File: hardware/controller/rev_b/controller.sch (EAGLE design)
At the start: 96 parts, among them J1 MODULE_CONTROLLER, J14 SOLDERJUMPERTRACE, J15 SOLDERJUMPERTRACE, J2 DM3AT-SF-PEJM5, J3 U.FL-R-SMT, J4 MICRO_USB_B_HIROSE_ZX62-B-5PA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, J5 MICRO_USB_B_HIROSE_ZX62-B-5PA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, J6 TC2030-JLINK-L, J7 TC2030-JLINK-L, J8 JUMPER-3PTH, Q1 MOSFET-NCHANNELSMD, Q2 NX3008PBK, SW1 PTS810SJ, SW2 SIP3240X, U1 SAM4LC8AA, U2 SAM4LC8AA, U3 RXM-GPS-RM-T, U4 FM25CLXXB-DG, U5 TS3USB30E, U6 FTDI234XD, U7 TXS0108EVQFN20, X1 16MHz, X2 16MHz

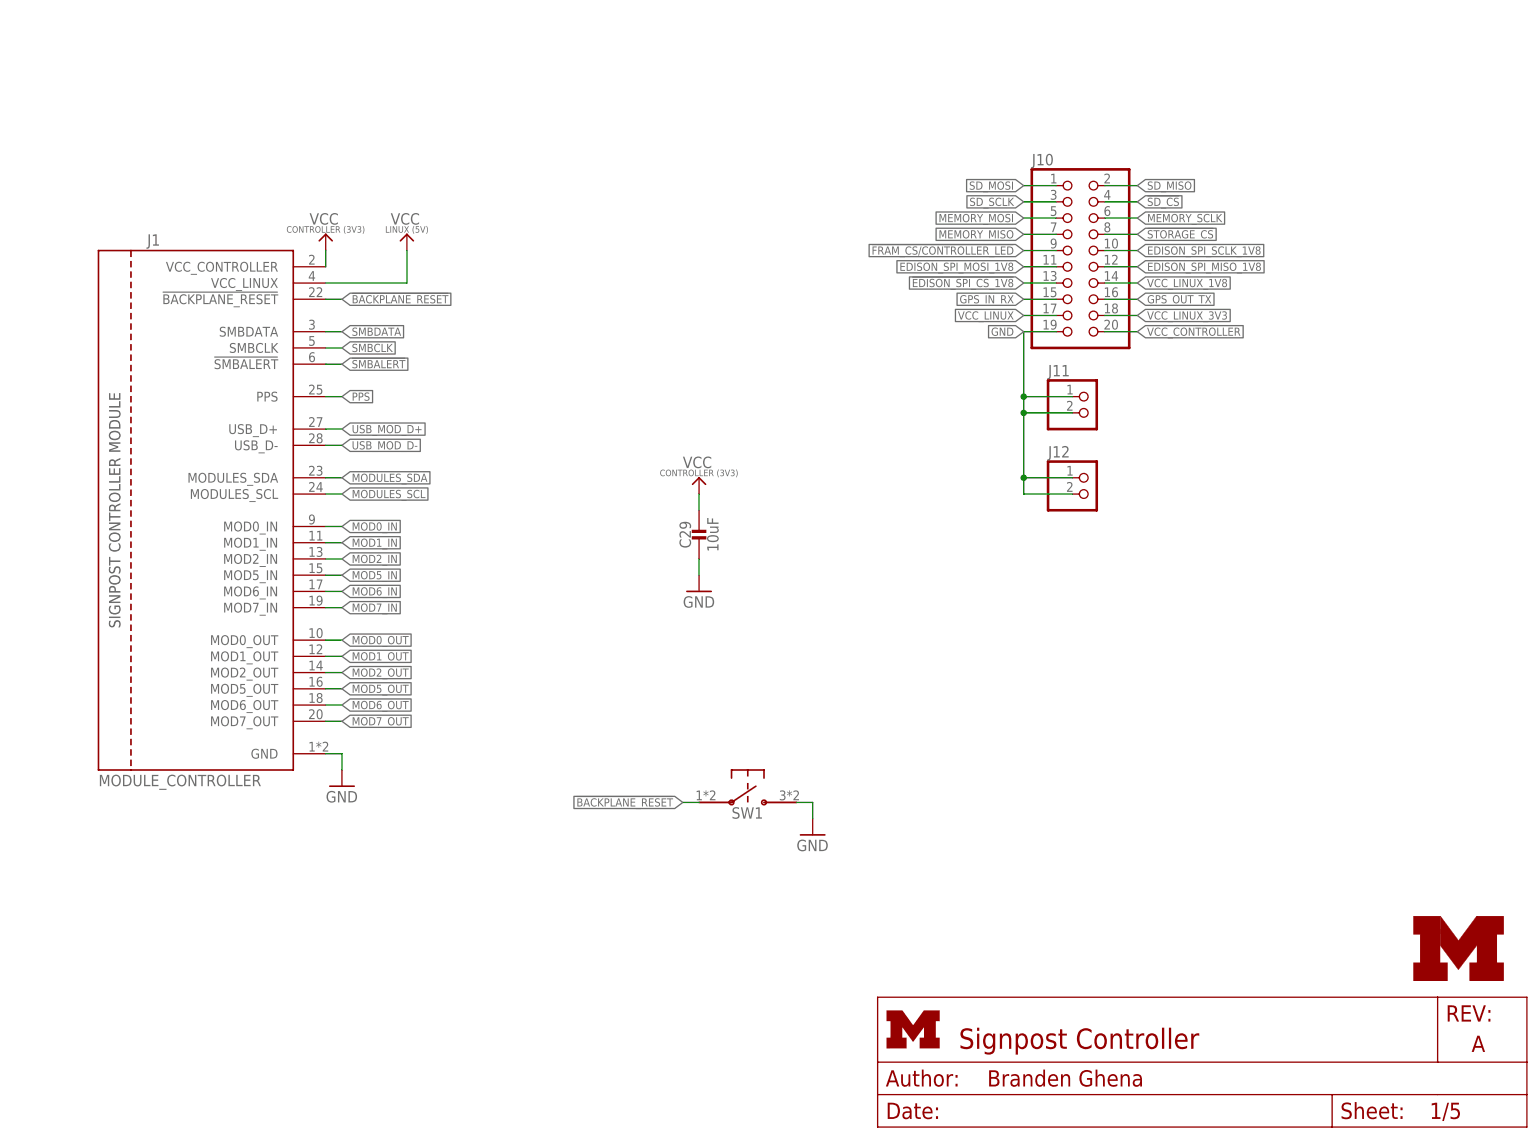
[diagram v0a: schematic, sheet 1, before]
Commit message: Created a debug header and added it to controller
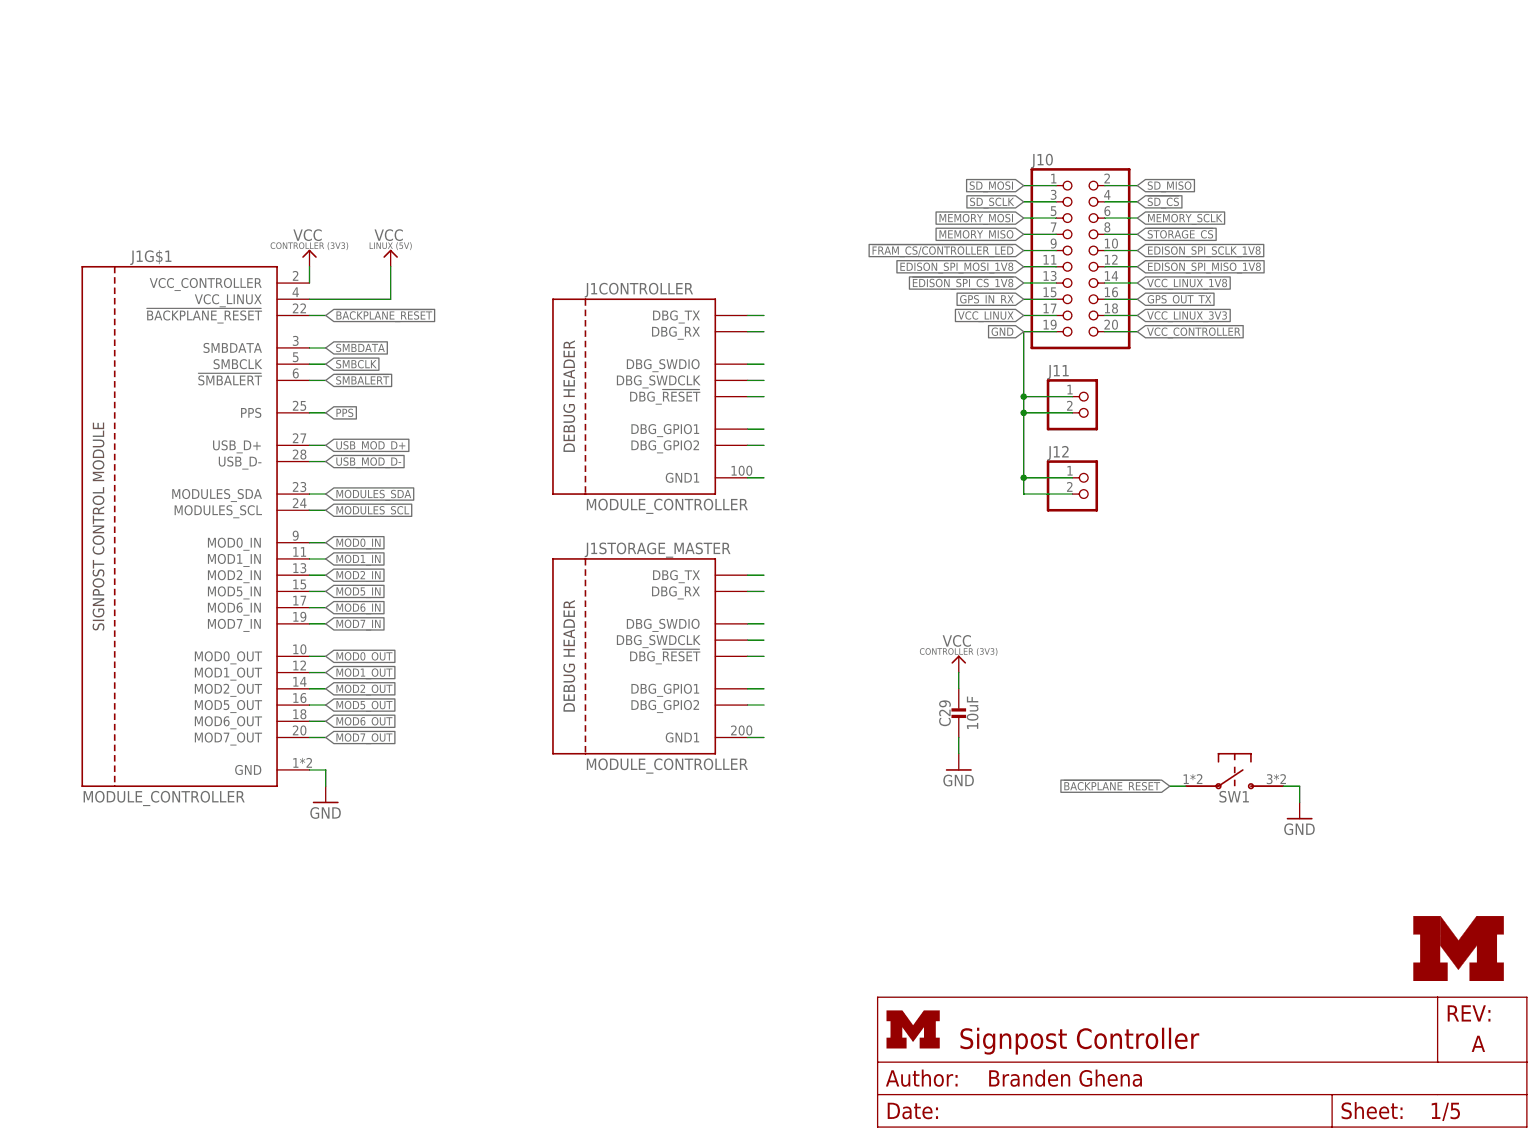
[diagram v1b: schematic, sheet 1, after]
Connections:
- new net N$19: J1CONTROLLER.DBG_TX
- new net N$20: J1CONTROLLER.DBG_RX
- new net N$21: J1CONTROLLER.DBG_SWDIO
- new net N$22: J1CONTROLLER.DBG_SWDCLK
- new net N$23: J1CONTROLLER.DBG_!RESET
- new net N$26: J1CONTROLLER.DBG_GPIO1
- new net N$27: J1CONTROLLER.DBG_GPIO2
- new net N$33: J1CONTROLLER.GND1
- new net N$35: J1STORAGE_MASTER.GND1
- new net N$36: J1STORAGE_MASTER.DBG_GPIO2
- new net N$39: J1STORAGE_MASTER.DBG_GPIO1
- new net N$40: J1STORAGE_MASTER.DBG_!RESET
- new net N$41: J1STORAGE_MASTER.DBG_SWDCLK
- new net N$42: J1STORAGE_MASTER.DBG_SWDIO
- new net N$47: J1STORAGE_MASTER.DBG_RX
- new net N$49: J1STORAGE_MASTER.DBG_TX
- net !BACKPLANE_RESET: now also J1G$1.!BACKPLANE_RESET; no longer J1.!BACKPLANE_RESET
- net !SMBALERT: now also J1G$1.!SMBALERT; no longer J1.!SMBALERT
- net GND: now also J1G$1.GND; no longer J1.GND
- net MOD0_IN: now also J1G$1.MOD0_IN; no longer J1.MOD0_IN
- net MOD0_OUT: now also J1G$1.MOD0_OUT; no longer J1.MOD0_OUT
- net MOD1_IN: now also J1G$1.MOD1_IN; no longer J1.MOD1_IN
- net MOD1_OUT: now also J1G$1.MOD1_OUT; no longer J1.MOD1_OUT
- net MOD2_IN: now also J1G$1.MOD2_IN; no longer J1.MOD2_IN
- net MOD2_OUT: now also J1G$1.MOD2_OUT; no longer J1.MOD2_OUT
- net MOD5_IN: now also J1G$1.MOD5_IN; no longer J1.MOD5_IN
- net MOD5_OUT: now also J1G$1.MOD5_OUT; no longer J1.MOD5_OUT
- net MOD6_IN: now also J1G$1.MOD6_IN; no longer J1.MOD6_IN
- net MOD6_OUT: now also J1G$1.MOD6_OUT; no longer J1.MOD6_OUT
- net MOD7_IN: now also J1G$1.MOD7_IN; no longer J1.MOD7_IN
- net MOD7_OUT: now also J1G$1.MOD7_OUT; no longer J1.MOD7_OUT
- net MODULES_SCL: now also J1G$1.MODULES_SCL; no longer J1.MODULES_SCL
- net MODULES_SDA: now also J1G$1.MODULES_SDA; no longer J1.MODULES_SDA
- net PPS: now also J1G$1.PPS; no longer J1.PPS
- net SMBCLK: now also J1G$1.SMBCLK; no longer J1.SMBCLK
- net SMBDATA: now also J1G$1.SMBDATA; no longer J1.SMBDATA
- net USB_MOD_D+: now also J1G$1.USB_D+; no longer J1.USB_D+
- net USB_MOD_D-: now also J1G$1.USB_D-; no longer J1.USB_D-
- net VCC_CONTROLLER: now also J1G$1.VCC_CONTROLLER; no longer J1.VCC_CONTROLLER
- net VCC_LINUX: now also J1G$1.VCC_LINUX; no longer J1.VCC_LINUX
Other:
- moved on the sheet: C29, J1G$1, SW1
